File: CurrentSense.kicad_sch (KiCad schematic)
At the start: 12 parts

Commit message: Basically done with schematic, will split to different PCBs now
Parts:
- C32, C33, C?: footprint (none) -> Capacitor_SMD:C_0805_2012Metric
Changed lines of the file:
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@@
       (effects (font (size 1.27 1.27)) (justify left))
     )
-    (property "Footprint" "" (at 154.305 49.53 0)
+    (property "Footprint" "Capacitor_SMD:C_0805_2012Metric" (at 154.305 49.53 0)
       (effects (font (size 1.27 1.27)) hide)
     )
@@
       (effects (font (size 1.27 1.27)) (justify left))
     )
-    (property "Footprint" "" (at 175.895 54.61 0)
+    (property "Footprint" "Capacitor_SMD:C_0805_2012Metric" (at 175.895 54.61 0)
       (effects (font (size 1.27 1.27)) hide)
     )
@@
       (effects (font (size 1.27 1.27)) (justify left))
     )
-    (property "Footprint" "" (at 138.43 71.12 0)
-      (effects (font (size 1.27 1.27)) hide)
-    )
+    (property "Footprint" "Capacitor_SMD:C_0805_2012Metric" (at 138.43 71.12 0)
+      (effects (font (size 1.27 1.27)) hide)
+    )

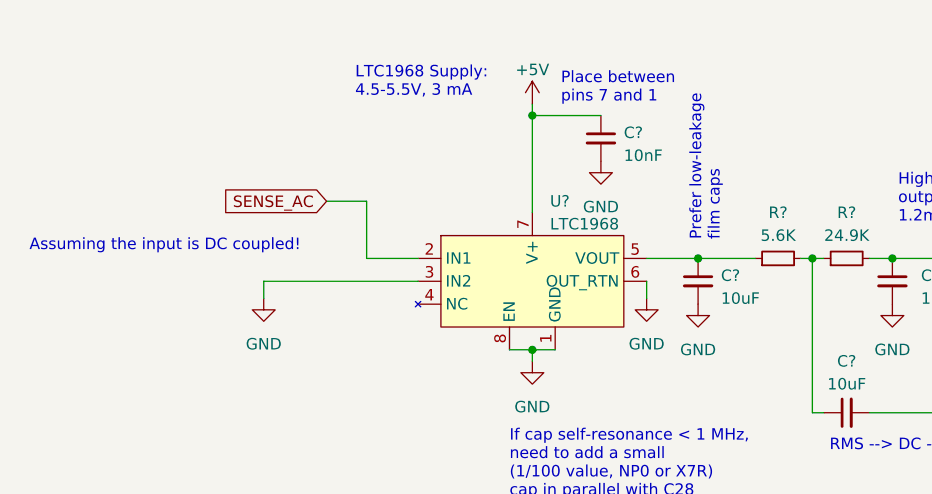
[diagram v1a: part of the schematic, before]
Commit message: Finished footprint assignment
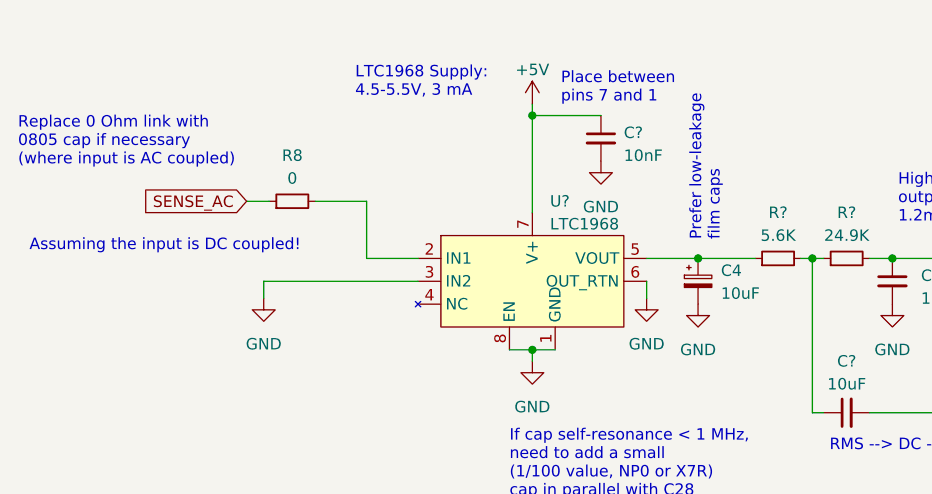
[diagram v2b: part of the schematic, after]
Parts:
- removed C?: 10uF, symbol Device:C_Small
- added C4: 10uF, Capacitor_Tantalum_SMD:CP_EIA-3216-18_Kemet-A, symbol Device:C_Polarized_Small
- added R8: 0, Resistor_SMD:R_0805_2012Metric, symbol Device:R_Small
- C? (x2): footprint (none) -> Capacitor_SMD:C_0805_2012Metric
- JP?: footprint (none) -> Jumper:SolderJumper-3_P1.3mm_Open_RoundedPad1.0x1.5mm
- R? (x2): footprint (none) -> Resistor_SMD:R_0805_2012Metric
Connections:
- net GND: now also C4.2
- net SENSE_AC: now also R8.1; no longer U?.2 (IN1)
- net at R?.1, U?.5 (VOUT): now also C4.1
- new net: R8.2, U?.2 (IN1)
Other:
- note added: "Replace 0 Ohm link with 0805 cap if necessary (where input is AC coupled)"
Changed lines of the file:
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@@
   (junction (at 170.815 71.12) (diameter 0) (color 0 0 0 0)
   )
+  (junction (at 116.84 68.58) (diameter 0) (color 0 0 0 0)
+  )
   (junction (at 138.43 68.58) (diameter 0) (color 0 0 0 0)
   )
   (junction (at 129.54 68.58) (diameter 0) (color 0 0 0 0)
   )
-  (junction (at 116.84 68.58) (diameter 0) (color 0 0 0 0)
-  )
   (junction (at 98.425 52.705) (diameter 0) (color 0 0 0 0)
   )
@@
     (stroke (width 0) (type default))
   )
-  (wire (pts (xy 75.565 62.23) (xy 80.01 62.23))
+  (wire (pts (xy 66.675 62.23) (xy 69.215 62.23))
     (stroke (width 0) (type default))
   )
@@
     (stroke (width 0) (type default))
   )
+  (wire (pts (xy 116.84 68.58) (xy 123.19 68.58))
+    (stroke (width 0) (type default))
+  )
   (wire (pts (xy 129.54 68.58) (xy 130.81 68.58))
     (stroke (width 0) (type default))
@@
     (stroke (width 0) (type default))
   )
-  (wire (pts (xy 116.84 68.58) (xy 123.19 68.58))
-    (stroke (width 0) (type default))
-  )
   (wire (pts (xy 98.425 80.01) (xy 98.425 78.74))
     (stroke (width 0) (type default))
@@
   )
   (wire (pts (xy 80.01 62.23) (xy 80.01 68.58))
+    (stroke (width 0) (type default))
+  )
+  (wire (pts (xy 74.295 62.23) (xy 80.01 62.23))
     (stroke (width 0) (type default))
   )
@@
   )
   (text "Assuming the input is DC coupled!" (at 42.545 67.945 0)
+    (effects (font (size 1.27 1.27)) (justify left bottom))
+  )
+  (text "Replace 0 Ohm link with\n0805 cap if necessary\n(where input is AC coupled)"
+    (at 41.275 58.42 0)
     (effects (font (size 1.27 1.27)) (justify left bottom))
   )
@@
     )
   )
-  (global_label "SENSE_AC" (shape input) (at 75.565 62.23 180) (fields_autoplaced)
+  (global_label "SENSE_AC" (shape input) (at 66.675 62.23 180) (fields_autoplaced)
     (effects (font (size 1.27 1.27)) (justify right))
-    (property "Intersheetrefs" "${INTERSHEET_REFS}" (at 63.2855 62.23 0)
+    (property "Intersheetrefs" "${INTERSHEET_REFS}" (at 54.3955 62.23 0)
       (effects (font (size 1.27 1.27)) (justify right) hide)
     )
@@
     )
   )
+  (symbol (lib_id "Device:C_Polarized_Small") (at 116.84 71.12 0) (unit 1)
+    (in_bom yes) (on_board yes) (dnp no) (fields_autoplaced)
+    (property "Reference" "C4" (at 119.38 69.9389 0)
+      (effects (font (size 1.27 1.27)) (justify left))
+    )
+    (property "Value" "10uF" (at 119.38 72.4789 0)
+      (effects (font (size 1.27 1.27)) (justify left))
+    )
+    (property "Footprint" "Capacitor_Tantalum_SMD:CP_EIA-3216-18_Kemet-A" (at 116.84 71.12 0)
+      (effects (font (size 1.27 1.27)) hide)
+    )
+    (property "Datasheet" "~" (at 116.84 71.12 0)
+      (effects (font (size 1.27 1.27)) hide)
+    )
+    (pin "1")
+    (pin "2")
+    (instances
+      (project "AMF-Generator"
+        (path "/c3df021c-646c-4a68-ac14-a081c2121d02/c9d53215-57f2-4e7d-aa5e-6d227a0ef0d2"
+          (reference "C4") (unit 1)
+        )
+      )
+    )
+  )
   (symbol (lib_id "Device:C_Small") (at 106.045 55.245 0) (unit 1)
     (in_bom yes) (on_board yes) (dnp no) (fields_autoplaced)
@@
       (effects (font (size 1.27 1.27)) (justify left))
     )
-    (property "Footprint" "" (at 106.045 55.245 0)
+    (property "Footprint" "Capacitor_SMD:C_0805_2012Metric" (at 106.045 55.245 0)
       (effects (font (size 1.27 1.27)) hide)
     )
@@
       (effects (font (size 1.27 1.27)) (justify left))
     )
-    (property "Footprint" "" (at 205.105 73.66 0)
+    (property "Footprint" "Jumper:SolderJumper-3_P1.3mm_Open_RoundedPad1.0x1.5mm" (at 205.105 73.66 0)
       (effects (font (size 1.27 1.27)) hide)
     )
@@
       (effects (font (size 1.27 1.27)))
     )
-    (property "Footprint" "" (at 133.35 68.58 0)
+    (property "Footprint" "Resistor_SMD:R_0805_2012Metric" (at 133.35 68.58 0)
       (effects (font (size 1.27 1.27)) hide)
     )
@@
       (effects (font (size 1.27 1.27)))
     )
-    (property "Footprint" "" (at 125.73 68.58 0)
+    (property "Footprint" "Resistor_SMD:R_0805_2012Metric" (at 125.73 68.58 0)
       (effects (font (size 1.27 1.27)) hide)
     )
@@
       (effects (font (size 1.27 1.27)))
     )
-    (property "Footprint" "" (at 133.35 85.725 0)
+    (property "Footprint" "Capacitor_SMD:C_0805_2012Metric" (at 133.35 85.725 0)
       (effects (font (size 1.27 1.27)) hide)
     )
@@
     )
   )
-  (symbol (lib_id "Device:C_Small") (at 116.84 71.12 0) (unit 1)
-    (in_bom yes) (on_board yes) (dnp no) (fields_autoplaced)
-    (property "Reference" "C?" (at 119.38 70.4913 0)
-      (effects (font (size 1.27 1.27)) (justify left))
-    )
-    (property "Value" "10uF" (at 119.38 73.0313 0)
-      (effects (font (size 1.27 1.27)) (justify left))
-    )
-    (property "Footprint" "" (at 116.84 71.12 0)
-      (effects (font (size 1.27 1.27)) hide)
-    )
-    (property "Datasheet" "~" (at 116.84 71.12 0)
-      (effects (font (size 1.27 1.27)) hide)
-    )
-    (pin "1")
-    (pin "2")
-    (instances
-      (project "AMF-Generator"
-        (path "/c3df021c-646c-4a68-ac14-a081c2121d02"
-          (reference "C?") (unit 1)
-        )
-        (path "/c3df021c-646c-4a68-ac14-a081c2121d02/c9d53215-57f2-4e7d-aa5e-6d227a0ef0d2"
-          (reference "C28") (unit 1)
-        )
-      )
+  (symbol (lib_id "Device:R_Small") (at 71.755 62.23 90) (unit 1)
+    (in_bom yes) (on_board yes) (dnp no) (fields_autoplaced)
+    (property "Reference" "R8" (at 71.755 57.15 90)
+      (effects (font (size 1.27 1.27)))
+    )
+    (property "Value" "0" (at 71.755 59.69 90)
+      (effects (font (size 1.27 1.27)))
+    )
+    (property "Footprint" "Resistor_SMD:R_0805_2012Metric" (at 71.755 62.23 0)
+      (effects (font (size 1.27 1.27)) hide)
+    )
+    (property "Datasheet" "~" (at 71.755 62.23 0)
+      (effects (font (size 1.27 1.27)) hide)
+    )
+    (pin "1")
+    (pin "2")
+    (instances
+      (project "AMF-Generator"
+        (path "/c3df021c-646c-4a68-ac14-a081c2121d02/c9d53215-57f2-4e7d-aa5e-6d227a0ef0d2"
+          (reference "R8") (unit 1)
+        )
+      )

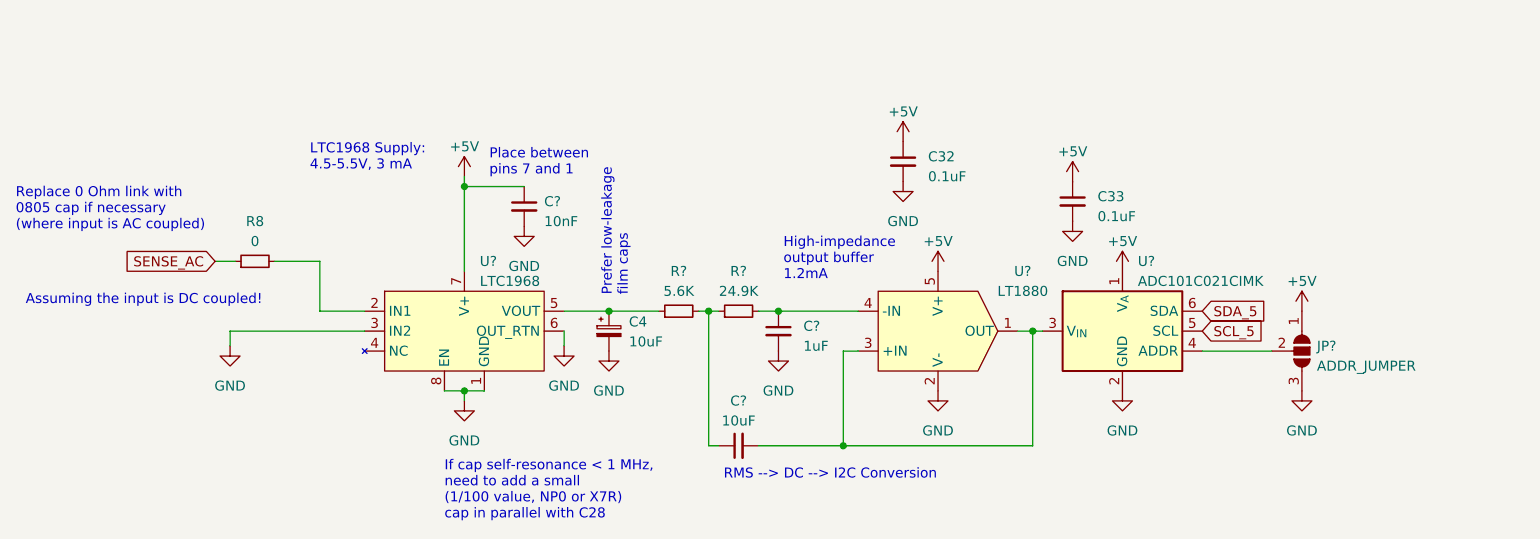
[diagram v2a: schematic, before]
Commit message: Initial pass of component placement complete. Added test points and i2c headers, also changed 12V input to terminal block
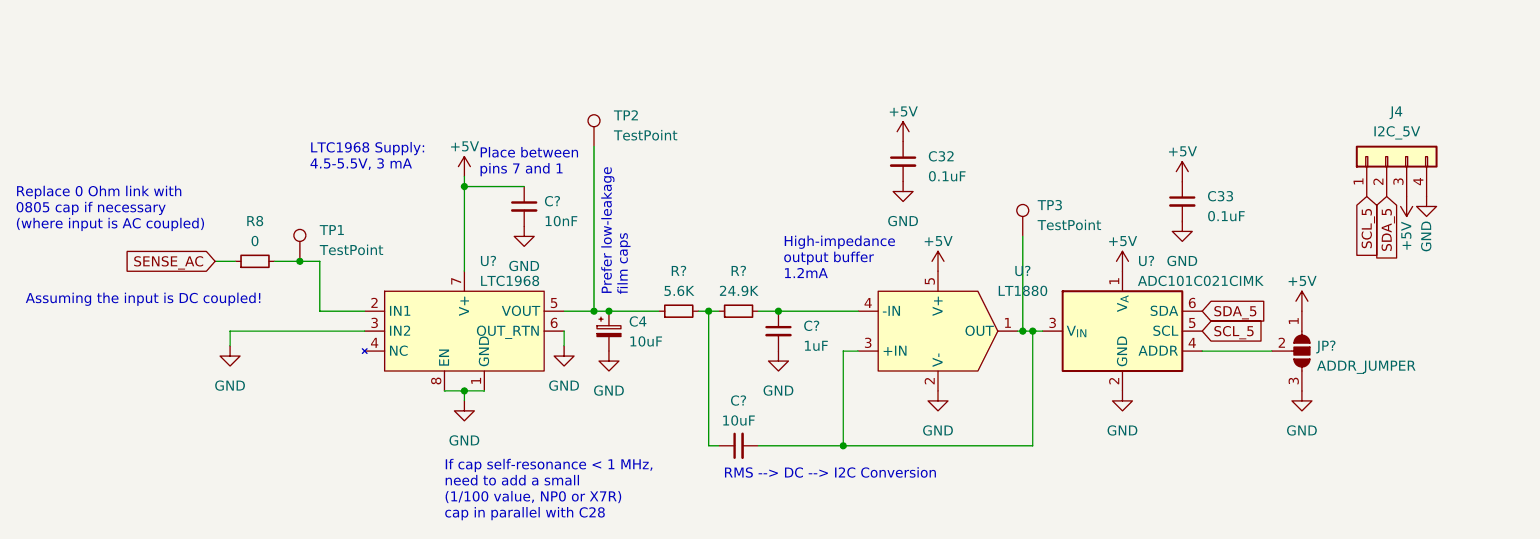
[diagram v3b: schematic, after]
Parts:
- added J4: I2C_5V, Connector_PinHeader_2.54mm:PinHeader_1x04_P2.54mm_Vertical, symbol Connector_Generic:Conn_01x04
- added TP1, TP2, TP3: TestPoint, TestPoint:TestPoint_THTPad_D2.0mm_Drill1.0mm, symbol Connector:TestPoint
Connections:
- net +5V: now also J4.3 (Pin_3)
- net GND: now also J4.4 (Pin_4)
- net SCL_5: now also J4.1 (Pin_1)
- net SDA_5: now also J4.2 (Pin_2)
- net at C4.1, R?.1, U?.5 (VOUT): now also TP2.1
- net at R8.2, U?.2 (IN1): now also TP1.1
- net at C?.2, U?.1 (OUT), U?.3 (+IN)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: now also TP3.1
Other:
- moved on the sheet: C33

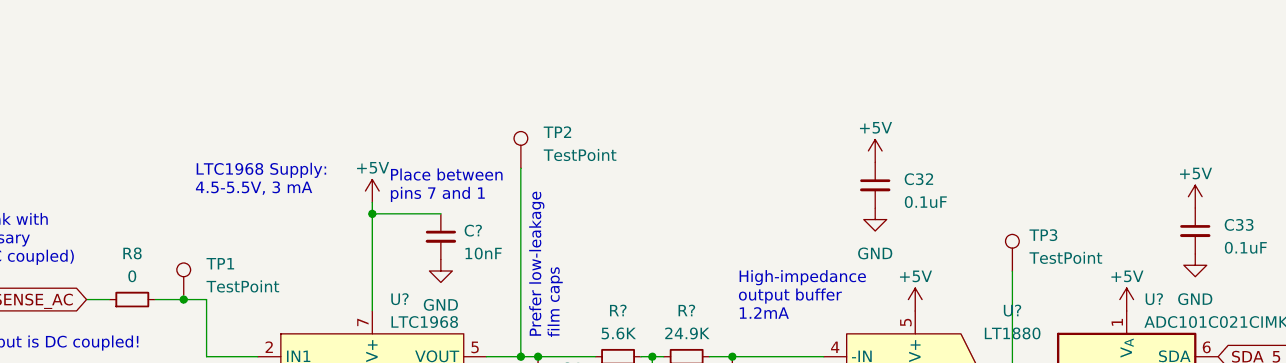
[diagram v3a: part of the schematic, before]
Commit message: Cleanup, changed board outline, DRC errors resolved
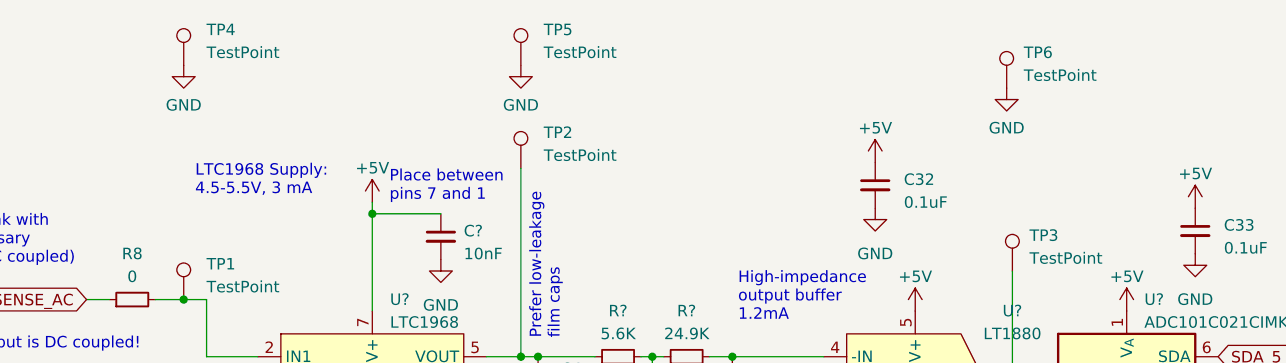
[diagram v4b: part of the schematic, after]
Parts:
- added TP4, TP5, TP6: TestPoint, TestPoint:TestPoint_THTPad_D2.0mm_Drill1.0mm, symbol Connector:TestPoint
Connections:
- net GND: now also TP4.1, TP5.1, TP6.1
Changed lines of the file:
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@@
+    )
+  )
+  (symbol (lib_id "Connector:TestPoint") (at 168.91 38.735 0) (unit 1)
+    (in_bom yes) (on_board yes) (dnp no) (fields_autoplaced)
+    (property "Reference" "TP6" (at 170.815 34.798 0)
+      (effects (font (size 1.27 1.27)) (justify left))
+    )
+    (property "Value" "TestPoint" (at 170.815 37.338 0)
+      (effects (font (size 1.27 1.27)) (justify left))
+    )
+    (property "Footprint" "TestPoint:TestPoint_THTPad_D2.0mm_Drill1.0mm" (at 173.99 38.735 0)
+      (effects (font (size 1.27 1.27)) hide)
+    )
+    (property "Datasheet" "~" (at 173.99 38.735 0)
+      (effects (font (size 1.27 1.27)) hide)
+    )
+    (pin "1")
+    (instances
+      (project "AMF-Generator"
+        (path "/c3df021c-646c-4a68-ac14-a081c2121d02/c9d53215-57f2-4e7d-aa5e-6d227a0ef0d2"
+          (reference "TP6") (unit 1)
+        )
+      )
     )
   )
@@
     )
   )
+  (symbol (lib_id "power:GND") (at 168.91 38.735 0) (unit 1)
+    (in_bom yes) (on_board yes) (dnp no) (fields_autoplaced)
+    (property "Reference" "#PWR074" (at 168.91 45.085 0)
+      (effects (font (size 1.27 1.27)) hide)
+    )
+    (property "Value" "GND" (at 168.91 43.18 0)
+      (effects (font (size 1.27 1.27)))
+    )
+    (property "Footprint" "" (at 168.91 38.735 0)
+      (effects (font (size 1.27 1.27)) hide)
+    )
+    (property "Datasheet" "" (at 168.91 38.735 0)
+      (effects (font (size 1.27 1.27)) hide)
+    )
+    (pin "1")
+    (instances
+      (project "AMF-Generator"
+        (path "/c3df021c-646c-4a68-ac14-a081c2121d02/c9d53215-57f2-4e7d-aa5e-6d227a0ef0d2"
+          (reference "#PWR074") (unit 1)
+        )
+      )
+    )
+  )
   (symbol (lib_id "power:GND") (at 189.865 57.15 0) (unit 1)
     (in_bom yes) (on_board yes) (dnp no) (fields_autoplaced)
@@
     )
   )
+  (symbol (lib_id "Connector:TestPoint") (at 77.47 36.195 0) (unit 1)
+    (in_bom yes) (on_board yes) (dnp no) (fields_autoplaced)
+    (property "Reference" "TP4" (at 80.01 32.258 0)
+      (effects (font (size 1.27 1.27)) (justify left))
+    )
+    (property "Value" "TestPoint" (at 80.01 34.798 0)
+      (effects (font (size 1.27 1.27)) (justify left))
+    )
+    (property "Footprint" "TestPoint:TestPoint_THTPad_D2.0mm_Drill1.0mm" (at 82.55 36.195 0)
+      (effects (font (size 1.27 1.27)) hide)
+    )
+    (property "Datasheet" "~" (at 82.55 36.195 0)
+      (effects (font (size 1.27 1.27)) hide)
+    )
+    (pin "1")
+    (instances
+      (project "AMF-Generator"
+        (path "/c3df021c-646c-4a68-ac14-a081c2121d02/c9d53215-57f2-4e7d-aa5e-6d227a0ef0d2"
+          (reference "TP4") (unit 1)
+        )
+      )
+    )
+  )
+  (symbol (lib_id "power:GND") (at 77.47 36.195 0) (unit 1)
+    (in_bom yes) (on_board yes) (dnp no) (fields_autoplaced)
+    (property "Reference" "#PWR076" (at 77.47 42.545 0)
+      (effects (font (size 1.27 1.27)) hide)
+    )
+    (property "Value" "GND" (at 77.47 40.64 0)
+      (effects (font (size 1.27 1.27)))
+    )
+    (property "Footprint" "" (at 77.47 36.195 0)
+      (effects (font (size 1.27 1.27)) hide)
+    )
+    (property "Datasheet" "" (at 77.47 36.195 0)
+      (effects (font (size 1.27 1.27)) hide)
+    )
+    (pin "1")
+    (instances
+      (project "AMF-Generator"
+        (path "/c3df021c-646c-4a68-ac14-a081c2121d02/c9d53215-57f2-4e7d-aa5e-6d227a0ef0d2"
+          (reference "#PWR076") (unit 1)
+        )
+      )
+    )
+  )
   (symbol (lib_id "power:GND") (at 154.305 52.07 0) (unit 1)
     (in_bom yes) (on_board yes) (dnp no) (fields_autoplaced)
@@
     )
   )
+  (symbol (lib_id "Connector:TestPoint") (at 114.935 36.195 0) (unit 1)
+    (in_bom yes) (on_board yes) (dnp no) (fields_autoplaced)
+    (property "Reference" "TP5" (at 117.475 32.258 0)
+      (effects (font (size 1.27 1.27)) (justify left))
+    )
+    (property "Value" "TestPoint" (at 117.475 34.798 0)
+      (effects (font (size 1.27 1.27)) (justify left))
+    )
+    (property "Footprint" "TestPoint:TestPoint_THTPad_D2.0mm_Drill1.0mm" (at 120.015 36.195 0)
+      (effects (font (size 1.27 1.27)) hide)
+    )
+    (property "Datasheet" "~" (at 120.015 36.195 0)
+      (effects (font (size 1.27 1.27)) hide)
+    )
+    (pin "1")
+    (instances
+      (project "AMF-Generator"
+        (path "/c3df021c-646c-4a68-ac14-a081c2121d02/c9d53215-57f2-4e7d-aa5e-6d227a0ef0d2"
+          (reference "TP5") (unit 1)
+        )
+      )
+    )
+  )
   (symbol (lib_id "power:GND") (at 68.58 73.025 0) (unit 1)
     (in_bom yes) (on_board yes) (dnp no) (fields_autoplaced)
@@
         )
       )
+    )
+  )
+  (symbol (lib_id "power:GND") (at 114.935 36.195 0) (unit 1)
+    (in_bom yes) (on_board yes) (dnp no) (fields_autoplaced)
+    (property "Reference" "#PWR075" (at 114.935 42.545 0)
+      (effects (font (size 1.27 1.27)) hide)
+    )
+    (property "Value" "GND" (at 114.935 40.64 0)
+      (effects (font (size 1.27 1.27)))
+    )
+    (property "Footprint" "" (at 114.935 36.195 0)
+      (effects (font (size 1.27 1.27)) hide)
+    )
+    (property "Datasheet" "" (at 114.935 36.195 0)
+      (effects (font (size 1.27 1.27)) hide)
+    )
+    (pin "1")
+    (instances
+      (project "AMF-Generator"
+        (path "/c3df021c-646c-4a68-ac14-a081c2121d02/c9d53215-57f2-4e7d-aa5e-6d227a0ef0d2"
+          (reference "#PWR075") (unit 1)
+        )
+      )
